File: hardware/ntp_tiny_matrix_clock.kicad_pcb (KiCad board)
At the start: 2 copper layers, 94 x 63 mm, 79 parts, among them J1 Barrel_Jack, J10 Conn_02x04_Odd_Even, J11 Conn_02x04_Odd_Even, J12 Conn_01x04_Male, J13 Conn_01x04_Male, J2 USB_B_Micro, J3 Conn_02x04_Odd_Even, J4 Conn_02x04_Odd_Even, J5 Conn_02x04_Odd_Even, J6 Conn_02x04_Odd_Even, J7 Conn_01x06_Male, J8 Conn_02x04_Odd_Even, J9 Conn_02x04_Odd_Even, Q1 Q_NPN_BEC, Q2 AO3401, Q3 AO3401, Q4 NJL7302L-F3, Q5 Q_NPN_BEC, Q6 Q_NPN_BEC, SW1 SW_PUSH_SMALL_H, U1 PCF8563, U2 NJW4132U2-C, U3 ESP32-WROOM, U4 W256064-XALG, U5 BME280, U7 JW5150A

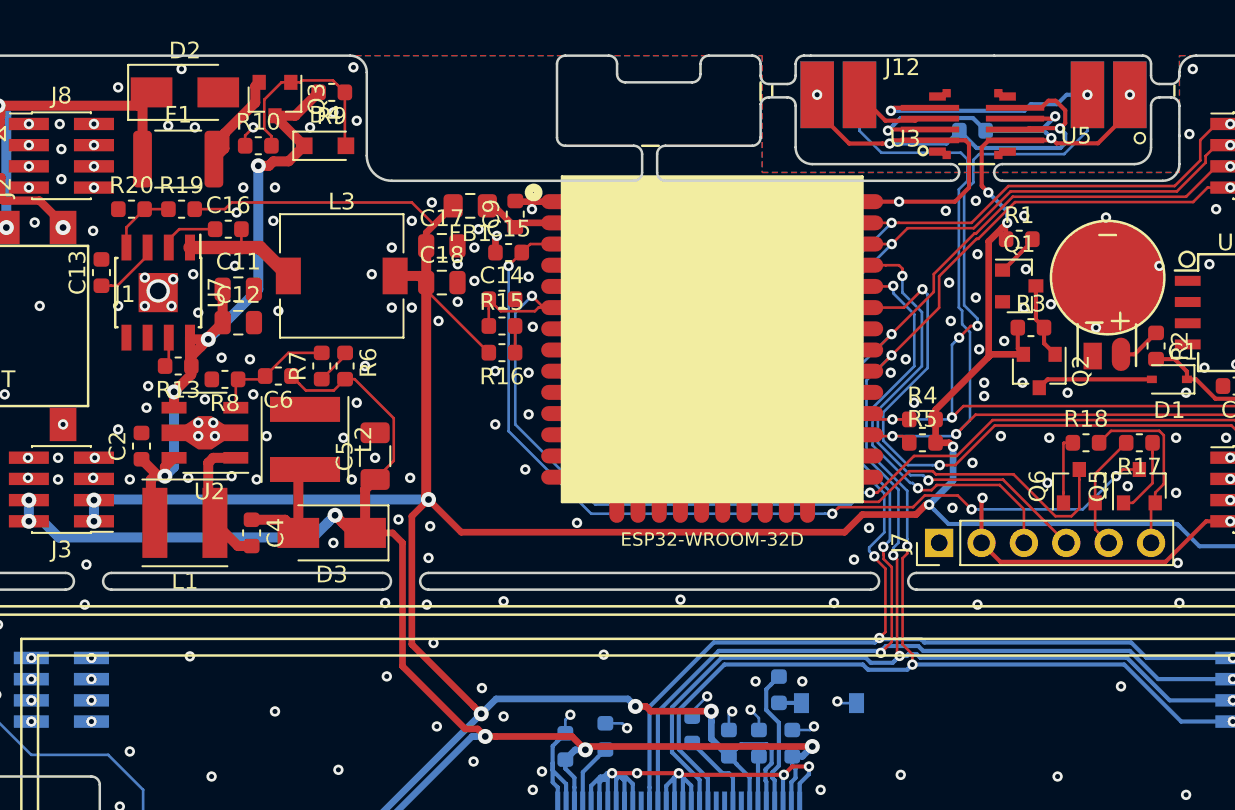
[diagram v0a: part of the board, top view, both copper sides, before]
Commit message: Layout and traces fix
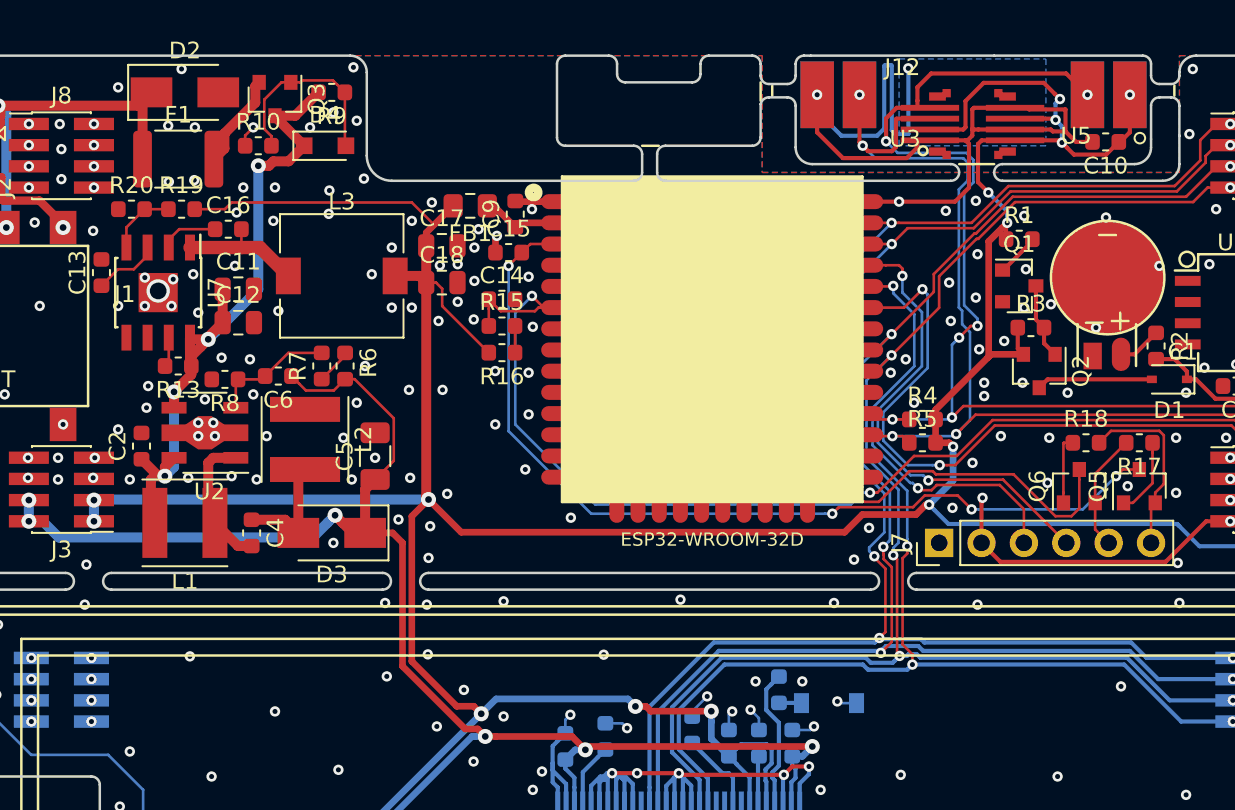
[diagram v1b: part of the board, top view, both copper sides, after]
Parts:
- C10: moved to F.Cu
- moved C10 8.01 mm to (89.6, 27.2)
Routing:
- net GND: track 180.3 -> 194.7 mm, vias 305 -> 314
- net SCL: track 103.3 -> 101.2 mm
- net SDA: track 90.9 -> 92.4 mm, vias 7 -> 9
- net +3V3: track 292.2 -> 293.1 mm

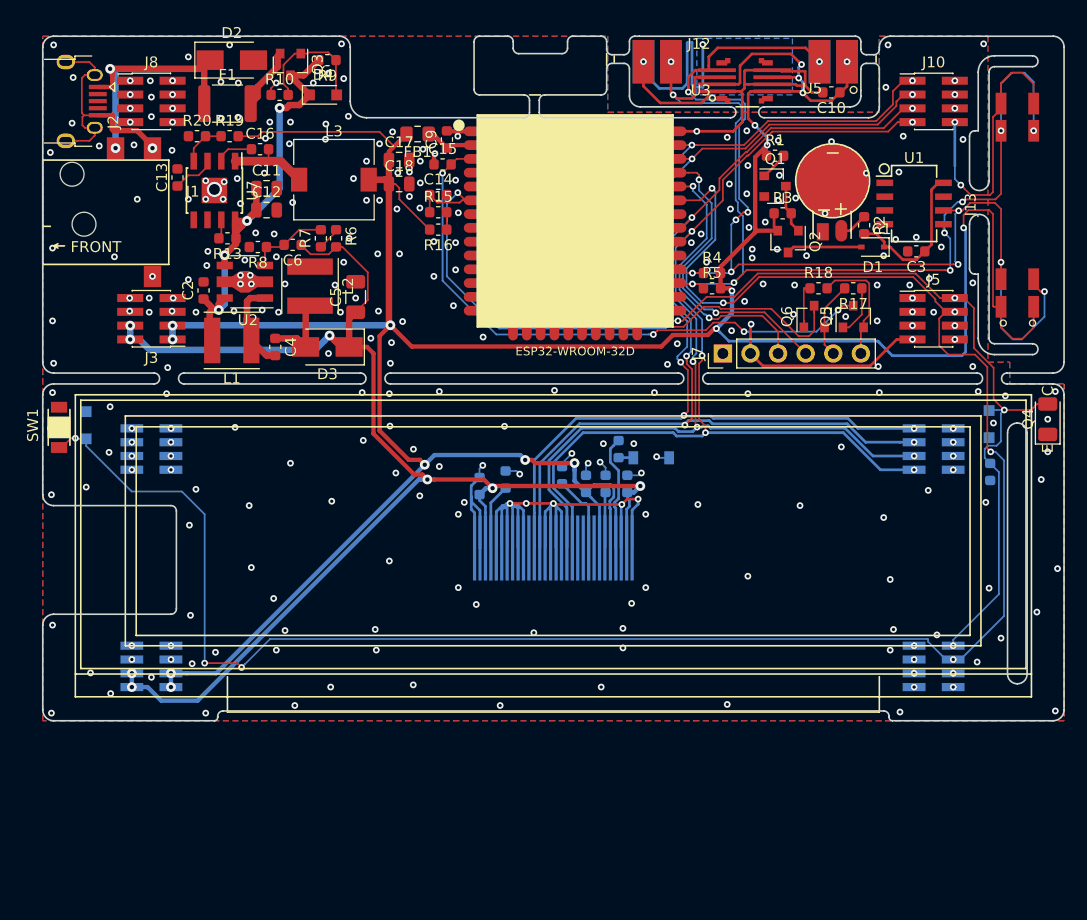
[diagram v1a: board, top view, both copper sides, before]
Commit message: to use holtek led driver
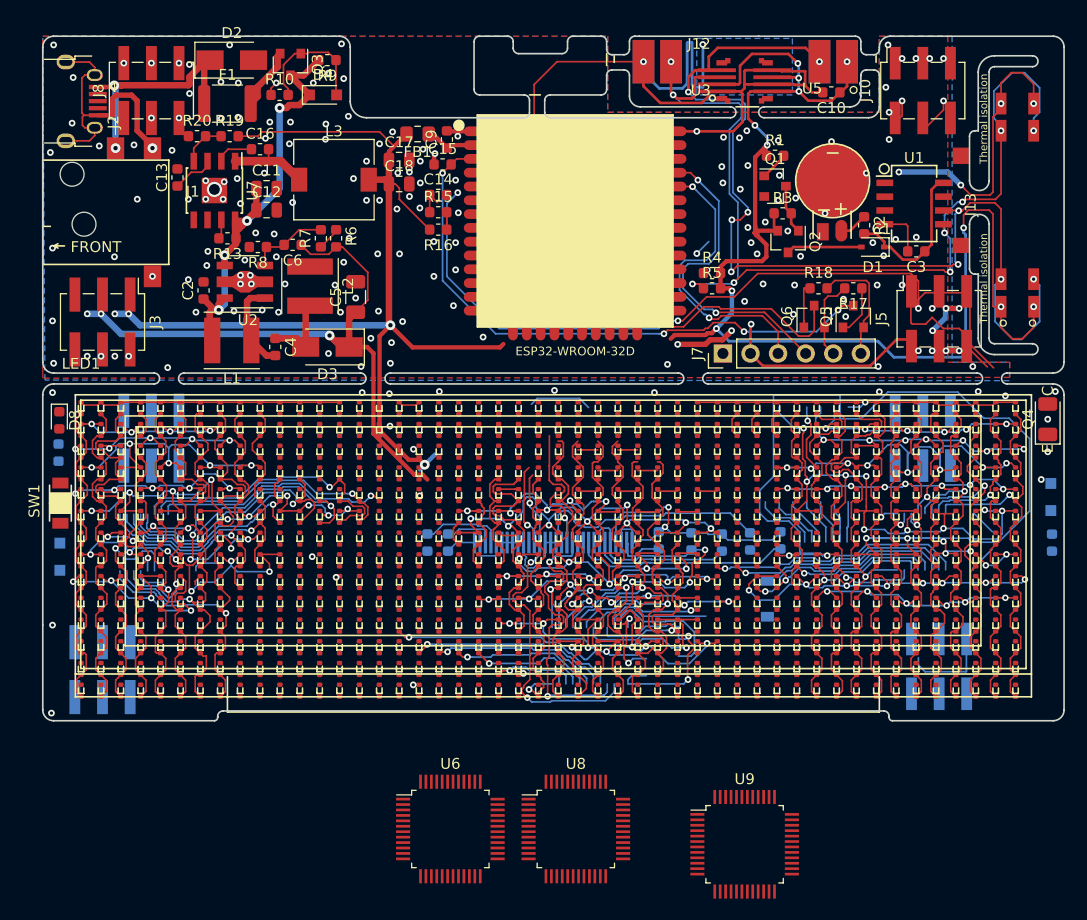
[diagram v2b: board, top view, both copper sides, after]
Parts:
- added D8: LED_Small, LED_SMD:LED_0603_1608Metric, F.Cu at (18.5, 57.4)
- added LED1: LED48x14, components:led_matrix_0402_48x14, F.Cu at (20.5, 56.2)
- added R21: 4.7k, Resistor_SMD:R_0603_1608Metric, B.Cu at (18.4, 60.3)
- added U6: HT16D35A, Package_QFP:LQFP-48_7x7mm_P0.5mm, F.Cu at (54.5, 95.0)
- added U8: HT16D35A, Package_QFP:LQFP-48_7x7mm_P0.5mm, F.Cu at (66.1, 95.0)
- added U9: HT16D35A, Package_QFP:LQFP-48_7x7mm_P0.5mm, F.Cu at (81.6, 96.4)
- J10, J5: footprint Connector_PinHeader_1.27mm:PinHeader_2x04_P1.27mm_Vertical_SMD -> Connector_PinSocket_2.54mm:PinSocket_2x03_P2.54mm_Vertical_SMD
- J11, J6: footprint Connector_PinSocket_1.27mm:PinSocket_2x04_P1.27mm_Vertical_SMD -> Connector_PinSocket_2.54mm:PinSocket_2x03_P2.54mm_Vertical_SMD
- J3, J8: footprint Connector_PinHeader_1.27mm:PinHeader_2x04_P1.27mm_Vertical_SMD -> Connector_PinHeader_2.54mm:PinHeader_2x03_P2.54mm_Vertical_SMD
- J4, J9: footprint Connector_PinSocket_1.27mm:PinSocket_2x04_P1.27mm_Vertical_SMD -> Connector_PinHeader_2.54mm:PinHeader_2x03_P2.54mm_Vertical_SMD
- moved R11 21.0 mm to (84.9, 68.4)
- moved D5 16.8 mm to (83.7, 73.8), turned to 90 degrees
- moved R12 14.8 mm to (82.1, 68.5)
- moved D6 12.3 mm to (18.6, 69.9)
- moved C21 12.0 mm to (79.5, 68.6)
- moved C19 11.1 mm to (76.7, 68.5)
- moved C8 9.25 mm to (52.4, 68.6), turned to 270 degrees
- moved D7 8.79 mm to (109.8, 64.4)
- moved R14 8.65 mm to (109.9, 68.6)
- moved SW1 6.98 mm to (18.6, 65.0)
- moved C7 5.95 mm to (73.7, 68.4)
- moved C20 5.95 mm to (54.3, 68.6), turned to 270 degrees
- moved J3 4.51 mm to (22.5, 48.3), turned to 270 degrees
- moved J4 4.51 mm to (22.5, 80.3), turned to 270 degrees
- moved J10 1.41 mm to (98.0, 27.0), turned to 90 degrees
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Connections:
- J10 pad 1: /LCDSPI_DAT -> GND
- J10 pad 2: GND -> LED_RLAT
- J10 pad 3: /LCDSPI_CLK -> GND
- J10 pad 4: GND -> LED_SCK
- J10 pad 5: /LCDSPI_D~C -> GND
- J10 pad 6: GND -> LED_SOUT
- J11 pad 1: /LCDSPI_DAT -> LED_RLAT
- J11 pad 3: /LCDSPI_CLK -> LED_SCK
- J11 pad 5: /LCDSPI_D~C -> LED_SOUT
- J3 pad 2: +12V -> GND
- J3 pad 4: +12V -> GND
- J3 pad 5: GND -> +12V
- J4 pad 2: GND -> +12V
- J4 pad 4: GND -> +3V3
- J4 pad 5: +12V -> GND
- J5 pad 1: GND -> E_AIN
- J5 pad 2: E_AIN -> GND
- J5 pad 3: GND -> E_BUTTON
- J5 pad 4: E_BUTTON -> GND
- J5 pad 5: GND -> LED_~SLAT
- J6 pad 1: GND -> LED_~SLAT
- J6 pad 3: GND -> E_BUTTON
- J6 pad 5: E_BUTTON -> E_AIN
- J8 pad 1: GND -> STATUS
- J9 pad 2: GND -> STATUS
- U3 pad 26: Net-(U3-Pad26) -> STATUS
- U3 pad 28: SCL -> Net-(U3-Pad28)
- U3 pad 29: Net-(U3-Pad29) -> LED_~SLAT
- U3 pad 30: /LCDSPI_CS -> LED_SOUT
- U3 pad 31: /LCDSPI_D~C -> LED_SCK
- U3 pad 33: E_BUTTON -> Net-(U3-Pad33)
- U3 pad 36: /LCDSPI_CLK -> Net-(U3-Pad36)
- U3 pad 37: /LCDSPI_DAT -> Net-(U3-Pad37)
- U3 pad 5: Net-(U3-Pad5) -> E_AIN
- U3 pad 6: E_AIN -> LED_SIN
- U3 pad 7: Net-(U3-Pad7) -> E_BUTTON
- U3 pad 8: Net-(U3-Pad8) -> LED_RLAT
- U4 pad 12: /LCDSPI_DAT -> LED_SOUT
- U4 pad 13: /LCDSPI_CLK -> LED_SCK
- U4 pad 18: /LCDSPI_D~C -> LED_RLAT
- U4 pad 19: /LCDSPI_CS -> LED_~SLAT
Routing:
- net /R7: track 0.00 -> 175.0 mm, vias 0 -> 21
- net E_BUTTON: track 182.6 -> 13.5 mm, vias 8 -> 1
- net /R5: track 0.00 -> 136.9 mm, vias 0 -> 24
- net /R8: track 0.00 -> 103.5 mm, vias 0 -> 18
- net /LCDSPI_DAT: track 98.4 -> 0.00 mm, vias 5 -> 0
- net /LCDSPI_CLK: track 96.5 -> 0.00 mm, vias 5 -> 0
- net /LCDSPI_D~C: track 93.7 -> 0.00 mm, vias 5 -> 0
- net /LCDSPI_CS: track 92.8 -> 0.00 mm, vias 5 -> 0
- net /R3: track 0.00 -> 82.4 mm, vias 0 -> 14
- net /R9: track 0.00 -> 69.9 mm, vias 0 -> 15
- net /R6: track 0.00 -> 69.4 mm, vias 0 -> 14
- net /R4: track 0.00 -> 66.3 mm, vias 0 -> 14
- net /R2: track 0.00 -> 62.9 mm, vias 0 -> 13
- net +12V: track 125.5 -> 66.4 mm, vias 8 -> 3
- net /R0: track 0.00 -> 58.0 mm, vias 0 -> 1
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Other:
- outline, holes or cut-outs redrawn
- net class Default: clearance 0.16 -> 0.15; trace_width 0.16 -> 0.15; via_dia 0.62 -> 0.6
- rule trace_clearance: 0.16 -> 0.15
- rule trace_min: 0.16 -> 0.15
- rule via_min_size: 0.62 -> 0.6
- board text added: "Thermal isolation"

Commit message: LED matrix circuit trace design ongoing. Too much difficult.
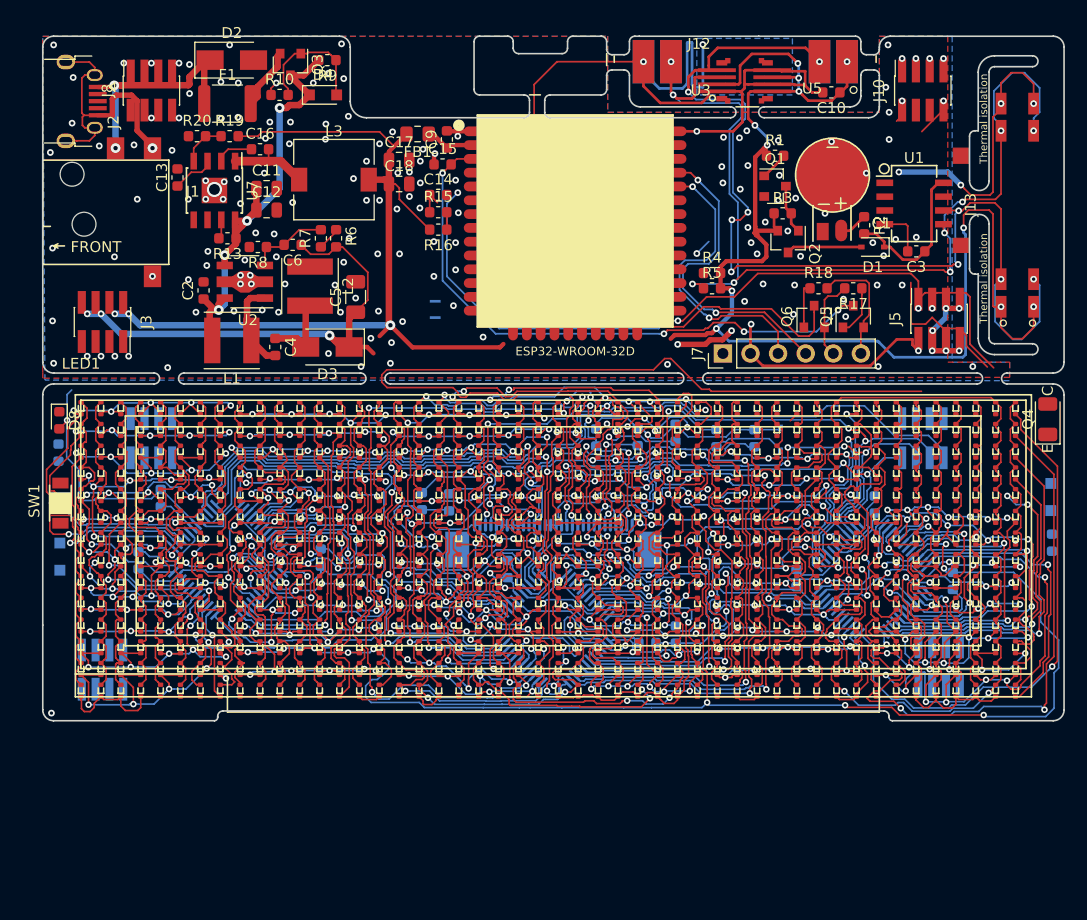
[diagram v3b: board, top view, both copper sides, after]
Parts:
- added C22: 1u/50V, Capacitor_SMD:C_0603_1608Metric, B.Cu at (100.8, 72.1)
- added C23: 1u/50V, Capacitor_SMD:C_0603_1608Metric, B.Cu at (93.6, 65.1)
- added C24: 1u/50V, Capacitor_SMD:C_0603_1608Metric, B.Cu at (75.3, 77.1)
- added C25: 1u/50V, Capacitor_SMD:C_0603_1608Metric, B.Cu at (59.8, 71.0)
- added C26: 1u/50V, Capacitor_SMD:C_0603_1608Metric, B.Cu at (42.6, 70.0)
- added C27: 1u/50V, Capacitor_SMD:C_0603_1608Metric, B.Cu at (27.9, 64.5)
- added JP1: Jumper_NC_Small, components:J_0.25mm, B.Cu at (53.1, 47.9)
- added JP2: Jumper_NC_Small, components:J_0.25mm, B.Cu at (53.1, 46.4)
- added R22: 1k, Resistor_SMD:R_0603_1608Metric, B.Cu at (25.8, 70.2)
- added R23: 1k, Resistor_SMD:R_0603_1608Metric, B.Cu at (72.7, 77.8)
- added R24: 1k, Resistor_SMD:R_0603_1608Metric, B.Cu at (86.4, 71.9)
- D5: footprint Diode_SMD:D_SOD-123 -> Diode_SMD:D_SOD-323
- J10, J11, J5, J6: footprint Connector_PinSocket_2.54mm:PinSocket_2x03_P2.54mm_Vertical_SMD -> Connector_PinSocket_1.27mm:PinSocket_2x04_P1.27mm_Vertical_SMD
- J3, J4, J8, J9: footprint Connector_PinHeader_2.54mm:PinHeader_2x03_P2.54mm_Vertical_SMD -> Connector_PinSocket_1.27mm:PinSocket_2x04_P1.27mm_Vertical_SMD
- LED1: footprint components:led_matrix_0402_48x14 -> thisproject:led_matrix_0402_48x14
- U6, U8, U9: moved to B.Cu
- moved U6 32.1 mm to (34.0, 70.2), turned to 315 degrees
- moved U9 27.1 mm to (93.3, 71.9), turned to 315 degrees
- moved U8 18.6 mm to (64.1, 76.5), turned to 315 degrees
- moved D5 14.7 mm to (84.9, 59.1), turned to 270 degrees
- moved C7 11.1 mm to (67.9, 58.9)
- moved C21 11.0 mm to (75.2, 58.5)
- moved C19 10.8 mm to (71.8, 58.9)
- moved R12 9.99 mm to (79.0, 59.0)
- moved R11 9.70 mm to (82.5, 59.0)
- moved C8 3.83 mm to (51.9, 64.8)
- moved C20 3.70 mm to (54.4, 64.9)
- moved C1 0.52 mm to (89.7, 39.5)
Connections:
- J2 pad 2: Net-(J2-Pad2) -> (no net)
- J2 pad 3: Net-(J2-Pad3) -> (no net)
- J2 pad 4: Net-(J2-Pad4) -> (no net)
- J4 pad 4: +3V3 -> +12V
- J5 pad 2: GND -> Net-(J5-Pad2)
- J5 pad 4: GND -> Net-(J5-Pad2)
- J5 pad 6: GND -> Net-(J5-Pad2)
- J6 pad 1: LED_~SLAT -> STATUS
- J6 pad 2: GND -> Net-(J5-Pad2)
- J6 pad 3: E_BUTTON -> LED_~SLAT
- J6 pad 4: GND -> Net-(J5-Pad2)
- J6 pad 5: E_AIN -> E_BUTTON
- J6 pad 6: GND -> Net-(J5-Pad2)
- J7 pad 1: Net-(J7-Pad1) -> (no net)
- J8 pad 1: STATUS -> /LEDVSS
- J8 pad 3: GND -> /LEDVSS
- J8 pad 5: GND -> /LEDVDD
- J9 pad 2: STATUS -> /LEDVSS
- J9 pad 4: GND -> /LEDVSS
- J9 pad 6: GND -> /LEDVDD
- U1 pad 1: Net-(U1-Pad1) -> (no net)
- U1 pad 2: Net-(U1-Pad2) -> (no net)
- U1 pad 3: Net-(U1-Pad3) -> (no net)
- U1 pad 7: Net-(U1-Pad7) -> (no net)
- U3 pad 10: Net-(U3-Pad10) -> (no net)
- U3 pad 11: Net-(U3-Pad11) -> (no net)
- U3 pad 12: Net-(U3-Pad12) -> (no net)
- U3 pad 13: Net-(U3-Pad13) -> (no net)
- U3 pad 14: Net-(U3-Pad14) -> (no net)
- U3 pad 16: Net-(U3-Pad16) -> (no net)
- U3 pad 17: Net-(U3-Pad17) -> (no net)
- U3 pad 18: Net-(U3-Pad18) -> (no net)
- U3 pad 19: Net-(U3-Pad19) -> (no net)
- U3 pad 20: Net-(U3-Pad20) -> (no net)
- U3 pad 21: Net-(U3-Pad21) -> (no net)
- U3 pad 22: Net-(U3-Pad22) -> (no net)
- U3 pad 23: Net-(U3-Pad23) -> (no net)
- U3 pad 24: Net-(U3-Pad24) -> (no net)
- U3 pad 28: Net-(U3-Pad28) -> (no net)
- U3 pad 32: Net-(U3-Pad32) -> (no net)
- U3 pad 33: Net-(U3-Pad33) -> (no net)
- U3 pad 36: Net-(U3-Pad36) -> (no net)
- U3 pad 37: Net-(U3-Pad37) -> (no net)
- U3 pad 4: Net-(U3-Pad4) -> (no net)
- U3 pad 6: LED_SIN -> (no net)
- U3 pad 9: Net-(U3-Pad9) -> (no net)
- U4 pad 11: Net-(U4-Pad11) -> (no net)
- U4 pad 20: Net-(U4-Pad20) -> (no net)
- U4 pad 21: Net-(U4-Pad21) -> (no net)
- U4 pad 23: Net-(U4-Pad23) -> (no net)
- U6 pad 1: Net-(U6-Pad1) -> /k0003
- U6 pad 10: Net-(U6-Pad10) -> LED_SCK
- U6 pad 11: Net-(U6-Pad11) -> /LEDSPI_CS0
- U6 pad 12: Net-(U6-Pad12) -> /LD_SYNC
- U6 pad 13: Net-(U6-Pad13) -> /a0000
- U6 pad 14: Net-(U6-Pad14) -> /LED_VDD
- U6 pad 15: Net-(U6-Pad15) -> /a0001
- U6 pad 16: Net-(U6-Pad16) -> /a0002
- U6 pad 17: Net-(U6-Pad17) -> /a0003
- U6 pad 18: Net-(U6-Pad18) -> /a0004
- U6 pad 19: Net-(U6-Pad19) -> /a0005
- U6 pad 2: Net-(U6-Pad2) -> /k0002
- U6 pad 20: Net-(U6-Pad20) -> /a0006
- U6 pad 21: Net-(U6-Pad21) -> /LED_VDD
- U6 pad 22: Net-(U6-Pad22) -> /a0007
- U6 pad 23: Net-(U6-Pad23) -> /k0027
- U6 pad 24: Net-(U6-Pad24) -> /k0026
- U6 pad 25: Net-(U6-Pad25) -> /k0025
- U6 pad 26: Net-(U6-Pad26) -> /k0024
- U6 pad 27: Net-(U6-Pad27) -> /k0023
- U6 pad 28: Net-(U6-Pad28) -> /LED_VSS
- U6 pad 29: Net-(U6-Pad29) -> /k0022
- U6 pad 3: Net-(U6-Pad3) -> /k0001
- U6 pad 30: Net-(U6-Pad30) -> /k0021
- U6 pad 31: Net-(U6-Pad31) -> /k0020
- U6 pad 32: Net-(U6-Pad32) -> /k0019
- U6 pad 33: Net-(U6-Pad33) -> /k0018
- U6 pad 34: Net-(U6-Pad34) -> /k0017
- U6 pad 35: Net-(U6-Pad35) -> /k0016
- U6 pad 36: Net-(U6-Pad36) -> /k0015
- U6 pad 37: Net-(U6-Pad37) -> /k0014
- U6 pad 38: Net-(U6-Pad38) -> /k0013
- U6 pad 39: Net-(U6-Pad39) -> /k0012
- U6 pad 4: Net-(U6-Pad4) -> /k0000
- U6 pad 40: Net-(U6-Pad40) -> /k0011
- U6 pad 41: Net-(U6-Pad41) -> /k0010
- U6 pad 42: Net-(U6-Pad42) -> /k0009
- U6 pad 43: Net-(U6-Pad43) -> /k0008
- U6 pad 44: Net-(U6-Pad44) -> /k0007
- U6 pad 45: Net-(U6-Pad45) -> /k0006
- U6 pad 46: Net-(U6-Pad46) -> /k0005
- U6 pad 47: Net-(U6-Pad47) -> /LED_VSS
- U6 pad 48: Net-(U6-Pad48) -> /k0004
- U6 pad 6: Net-(U6-Pad6) -> GND
- U6 pad 7: Net-(U6-Pad7) -> +3V3
- U6 pad 8: Net-(U6-Pad8) -> /LD_OSC
- U6 pad 9: Net-(U6-Pad9) -> LED_SOUT
- U7 pad 5: Net-(U7-Pad5) -> (no net)
- U7 pad 6: Net-(U7-Pad6) -> (no net)
- U8 pad 1: Net-(U8-Pad1) -> /k0103
- U8 pad 10: Net-(U8-Pad10) -> LED_SCK
- U8 pad 11: Net-(U8-Pad11) -> LED_~SLAT
- U8 pad 12: Net-(U8-Pad12) -> /LD_SYNC
- U8 pad 13: Net-(U8-Pad13) -> /a0100
- U8 pad 14: Net-(U8-Pad14) -> /LED_VDD
- U8 pad 15: Net-(U8-Pad15) -> /a0101
- U8 pad 16: Net-(U8-Pad16) -> /a0102
- U8 pad 17: Net-(U8-Pad17) -> /a0103
- U8 pad 18: Net-(U8-Pad18) -> /a0104
- U8 pad 19: Net-(U8-Pad19) -> /a0105
- U8 pad 2: Net-(U8-Pad2) -> /k0102
- U8 pad 20: Net-(U8-Pad20) -> /a0106
- U8 pad 21: Net-(U8-Pad21) -> /LED_VDD
- U8 pad 22: Net-(U8-Pad22) -> /a0107
- U8 pad 23: Net-(U8-Pad23) -> /k0127
- U8 pad 24: Net-(U8-Pad24) -> /k0126
- U8 pad 25: Net-(U8-Pad25) -> /k0125
- U8 pad 26: Net-(U8-Pad26) -> /k0124
- U8 pad 27: Net-(U8-Pad27) -> /k0123
- U8 pad 28: Net-(U8-Pad28) -> /LED_VSS
- U8 pad 29: Net-(U8-Pad29) -> /k0122
- U8 pad 3: Net-(U8-Pad3) -> /k0101
- U8 pad 30: Net-(U8-Pad30) -> /k0121
- U8 pad 31: Net-(U8-Pad31) -> /k0120
- U8 pad 32: Net-(U8-Pad32) -> /k0119
- U8 pad 33: Net-(U8-Pad33) -> /k0118
- U8 pad 34: Net-(U8-Pad34) -> /k0117
- U8 pad 35: Net-(U8-Pad35) -> /k0116
- U8 pad 36: Net-(U8-Pad36) -> /k0115
- U8 pad 37: Net-(U8-Pad37) -> /k0114
- U8 pad 38: Net-(U8-Pad38) -> /k0113
- U8 pad 39: Net-(U8-Pad39) -> /k0112
- U8 pad 4: Net-(U8-Pad4) -> /k0100
- U8 pad 40: Net-(U8-Pad40) -> /k0111
- U8 pad 41: Net-(U8-Pad41) -> /k0110
- U8 pad 42: Net-(U8-Pad42) -> /k0109
- U8 pad 43: Net-(U8-Pad43) -> /k0108
- U8 pad 44: Net-(U8-Pad44) -> /k0107
- U8 pad 45: Net-(U8-Pad45) -> /k0106
- U8 pad 46: Net-(U8-Pad46) -> /k0105
- U8 pad 47: Net-(U8-Pad47) -> /LED_VSS
- U8 pad 48: Net-(U8-Pad48) -> /k0104
- U8 pad 6: Net-(U8-Pad6) -> GND
- U8 pad 7: Net-(U8-Pad7) -> +3V3
- U8 pad 8: Net-(U8-Pad8) -> /LD_OSC
- U8 pad 9: Net-(U8-Pad9) -> LED_SOUT
- U9 pad 1: Net-(U9-Pad1) -> /k0203
- U9 pad 10: Net-(U9-Pad10) -> LED_SCK
- U9 pad 11: Net-(U9-Pad11) -> LED_RLAT
- U9 pad 12: Net-(U9-Pad12) -> /LD_SYNC
- U9 pad 13: Net-(U9-Pad13) -> /a0200
- U9 pad 14: Net-(U9-Pad14) -> /LED_VDD
- U9 pad 15: Net-(U9-Pad15) -> /a0201
- U9 pad 16: Net-(U9-Pad16) -> /a0202
- U9 pad 17: Net-(U9-Pad17) -> /a0203
- U9 pad 18: Net-(U9-Pad18) -> /a0204
- U9 pad 19: Net-(U9-Pad19) -> /a0205
- U9 pad 2: Net-(U9-Pad2) -> /k0202
- U9 pad 20: Net-(U9-Pad20) -> /a0206
- U9 pad 21: Net-(U9-Pad21) -> /LED_VDD
- U9 pad 22: Net-(U9-Pad22) -> /a0207
- U9 pad 23: Net-(U9-Pad23) -> /k0227
- U9 pad 24: Net-(U9-Pad24) -> /k0226
- U9 pad 25: Net-(U9-Pad25) -> /k0225
- U9 pad 26: Net-(U9-Pad26) -> /k0224
- U9 pad 27: Net-(U9-Pad27) -> /k0223
- U9 pad 28: Net-(U9-Pad28) -> /LED_VSS
- U9 pad 29: Net-(U9-Pad29) -> /k0222
- U9 pad 3: Net-(U9-Pad3) -> /k0201
- U9 pad 30: Net-(U9-Pad30) -> /k0221
- U9 pad 31: Net-(U9-Pad31) -> /k0220
- U9 pad 32: Net-(U9-Pad32) -> /k0219
- U9 pad 33: Net-(U9-Pad33) -> /k0218
- U9 pad 34: Net-(U9-Pad34) -> /k0217
- U9 pad 35: Net-(U9-Pad35) -> /k0216
- U9 pad 36: Net-(U9-Pad36) -> /k0215
- U9 pad 37: Net-(U9-Pad37) -> /k0214
- U9 pad 38: Net-(U9-Pad38) -> /k0213
- U9 pad 39: Net-(U9-Pad39) -> /k0212
- U9 pad 4: Net-(U9-Pad4) -> /k0200
- U9 pad 40: Net-(U9-Pad40) -> /k0211
- U9 pad 41: Net-(U9-Pad41) -> /k0210
- U9 pad 42: Net-(U9-Pad42) -> /k0209
- U9 pad 43: Net-(U9-Pad43) -> /k0208
- U9 pad 44: Net-(U9-Pad44) -> /k0207
- U9 pad 45: Net-(U9-Pad45) -> /k0206
- U9 pad 46: Net-(U9-Pad46) -> /k0205
- U9 pad 47: Net-(U9-Pad47) -> /LED_VSS
- U9 pad 48: Net-(U9-Pad48) -> /k0204
- U9 pad 6: Net-(U9-Pad6) -> GND
- U9 pad 7: Net-(U9-Pad7) -> +3V3
- U9 pad 8: Net-(U9-Pad8) -> /LD_OSC
- U9 pad 9: Net-(U9-Pad9) -> LED_SOUT
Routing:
- net /R7: track 175.0 -> 0.00 mm, vias 21 -> 0
- net /LED_VDD: track 0.00 -> 159.2 mm, vias 0 -> 10
- net /R5: track 136.9 -> 0.00 mm, vias 24 -> 0
- net /a0206: track 0.00 -> 110.4 mm, vias 0 -> 3
- net /a0101: track 0.00 -> 105.1 mm, vias 0 -> 5
- net /LED_VSS: track 0.00 -> 104.4 mm, vias 0 -> 6
- net /a0106: track 0.00 -> 104.3 mm, vias 0 -> 3
- net /R8: track 103.5 -> 0.00 mm, vias 18 -> 0
- net /a0102: track 0.00 -> 99.1 mm, vias 0 -> 3
- net /a0104: track 0.00 -> 94.5 mm, vias 0 -> 5
- net /a0105: track 0.00 -> 92.2 mm, vias 0 -> 3
- net /a0107: track 0.00 -> 91.6 mm, vias 0 -> 4
- net LED_SOUT: track 13.4 -> 105.0 mm, vias 1 -> 2
- net /k0114: track 0.00 -> 90.3 mm, vias 0 -> 10
- net /a0103: track 0.00 -> 89.8 mm, vias 0 -> 5
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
